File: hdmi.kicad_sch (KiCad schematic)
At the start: 43 parts, among them J13 WE_685119136923_alt_sym, Q1 PJE138K, Q12 PJE138K, U36 TS3DV642RUARQ1, U43 NTS0102GT, U44 TPD4E05U06QDQARQ1, U45 TPD4E05U06QDQARQ1, U46 TPD4E05U06QDQARQ1

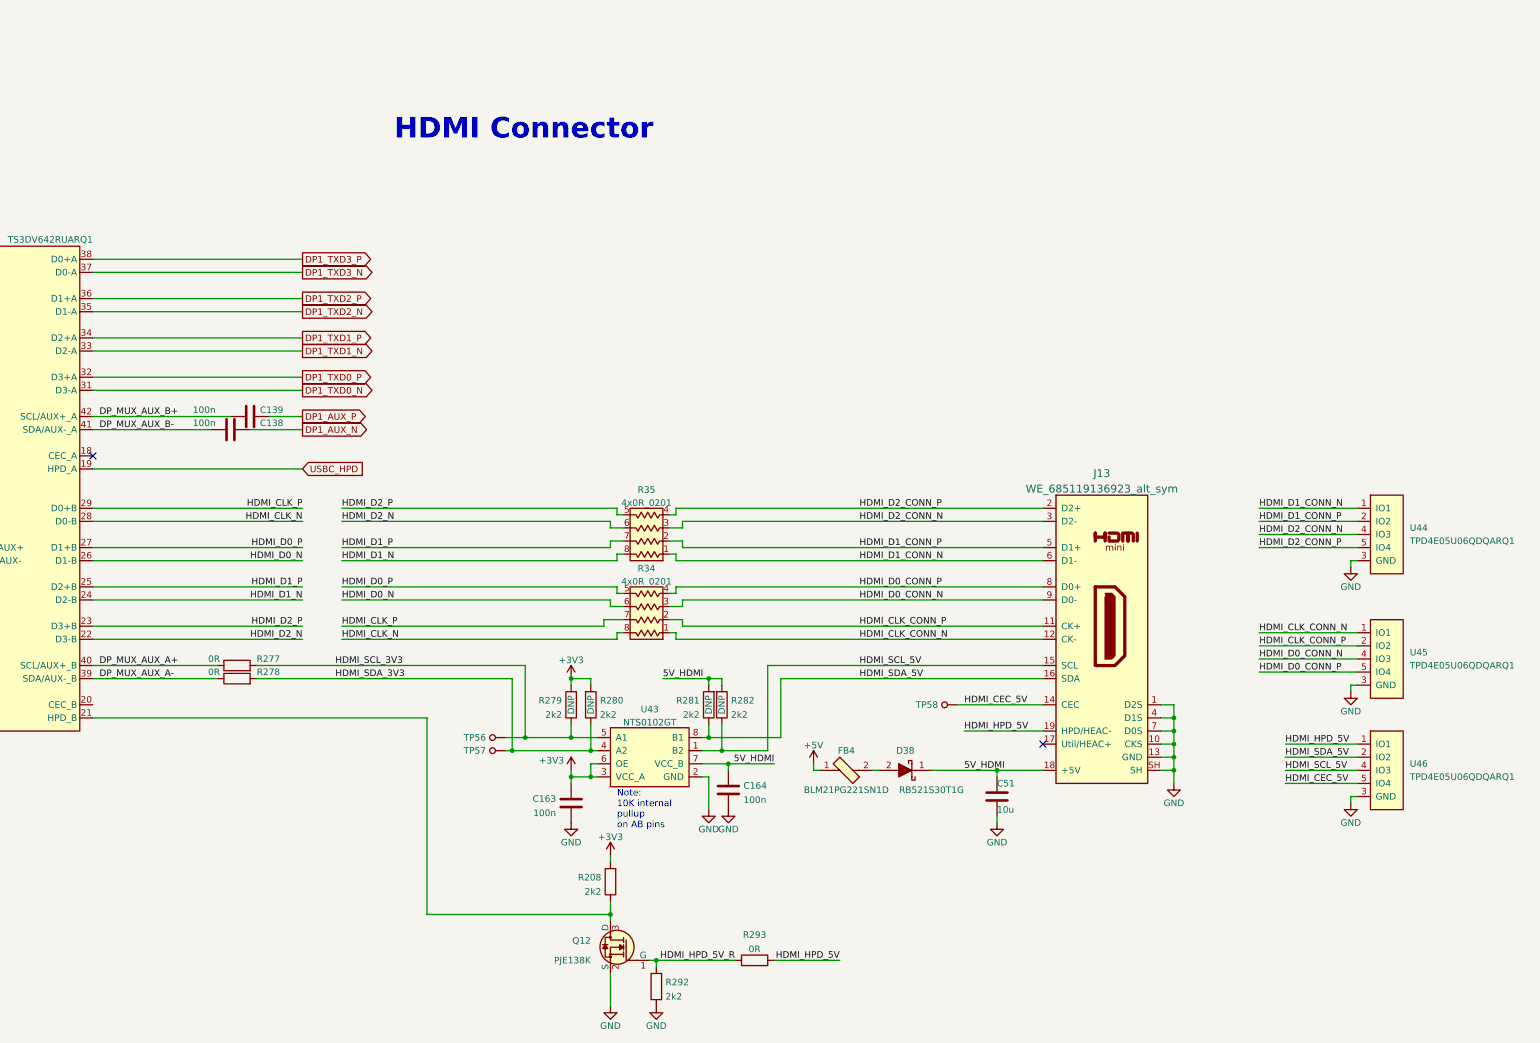
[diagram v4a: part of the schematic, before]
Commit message: Added 499 Ohm resistors required for HDMI
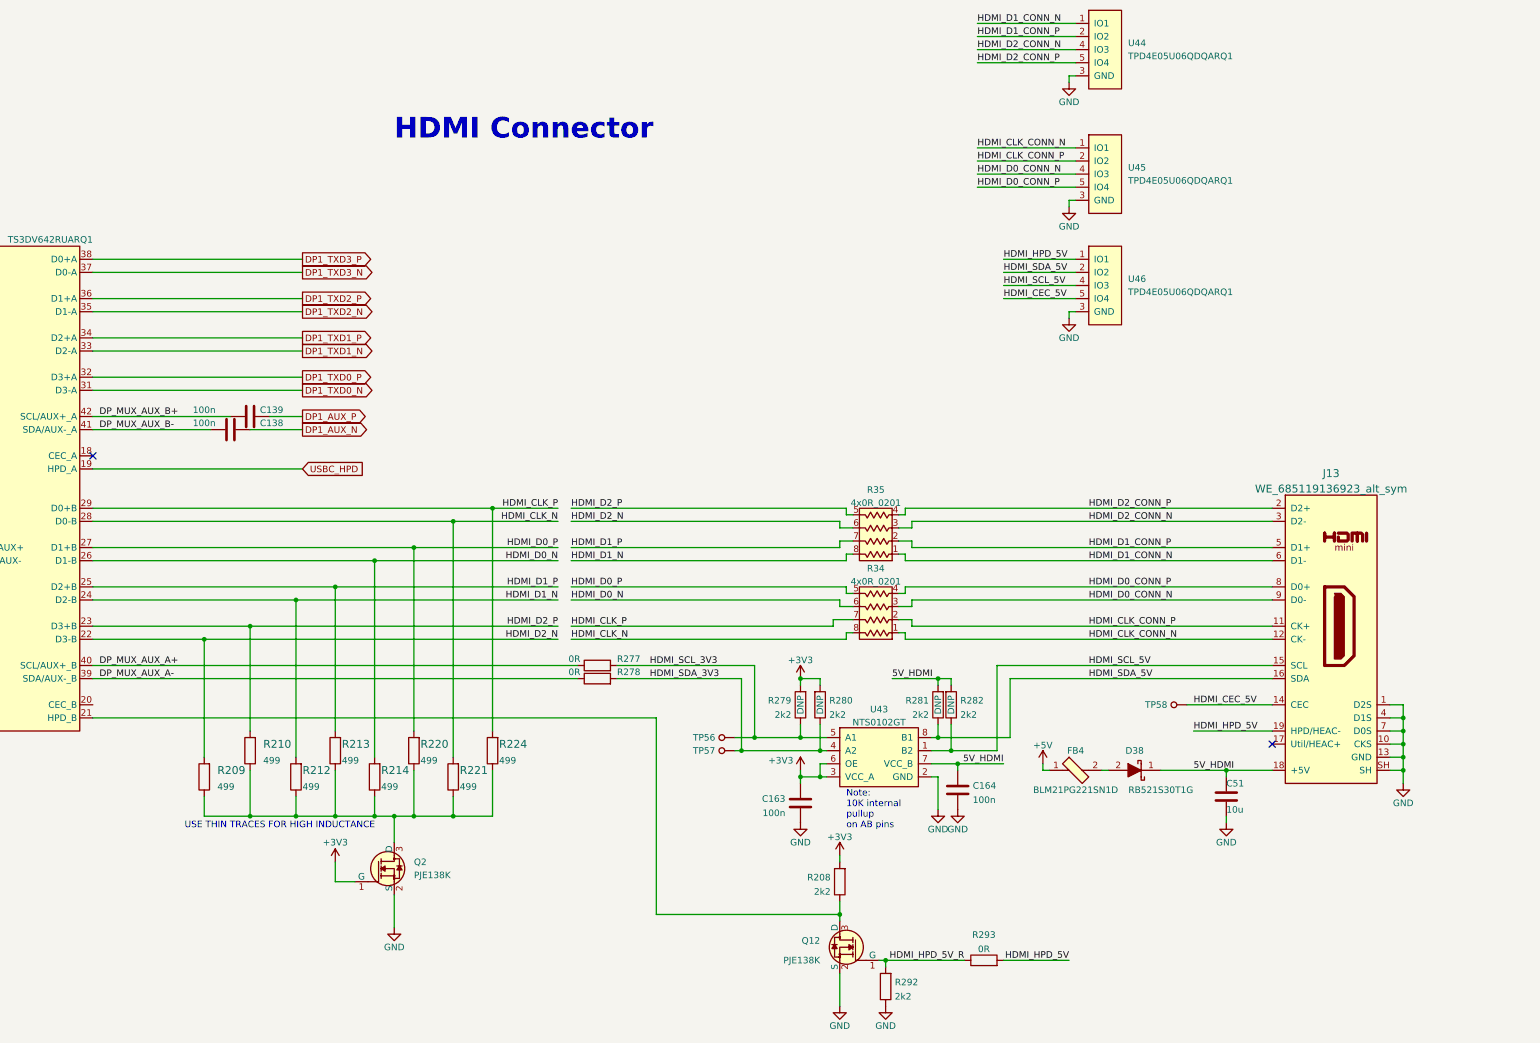
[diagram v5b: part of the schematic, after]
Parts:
- added Q2: PJE138K, antmicro-footprints:SOT-523, symbol antmicroTransistorsFETsMOSFETsSingle:PJE138K
- added R209, R210, R212, R213, R214, R220, R221, R224: R_499_0402, antmicro-footprints:0402-res, symbol antmicroResistors0402:R_499_0402
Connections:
- net +3V3: now also Q2.1 (G)
- net GND: now also Q2.2 (S)
- net HDMI_CLK_N: now also R221.2
- net HDMI_CLK_P: now also R224.2
- net HDMI_D0_N: now also R214.2
- net HDMI_D0_P: now also R220.2
- net HDMI_D1_N: now also R212.2
- net HDMI_D1_P: now also R213.2
- net HDMI_D2_N: now also R209.2
- net HDMI_D2_P: now also R210.2
- new net: Q2.3 (D), R209.1, R210.1, R212.1, R213.1, R214.1, R220.1, R221.1, R224.1
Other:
- note added: "USE THIN TRACES FOR HIGH INDUCTANCE"
- moved on the sheet: C163, C164, C51, D38, FB4, J13, Q12, R208, R277, R278, R279, R280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

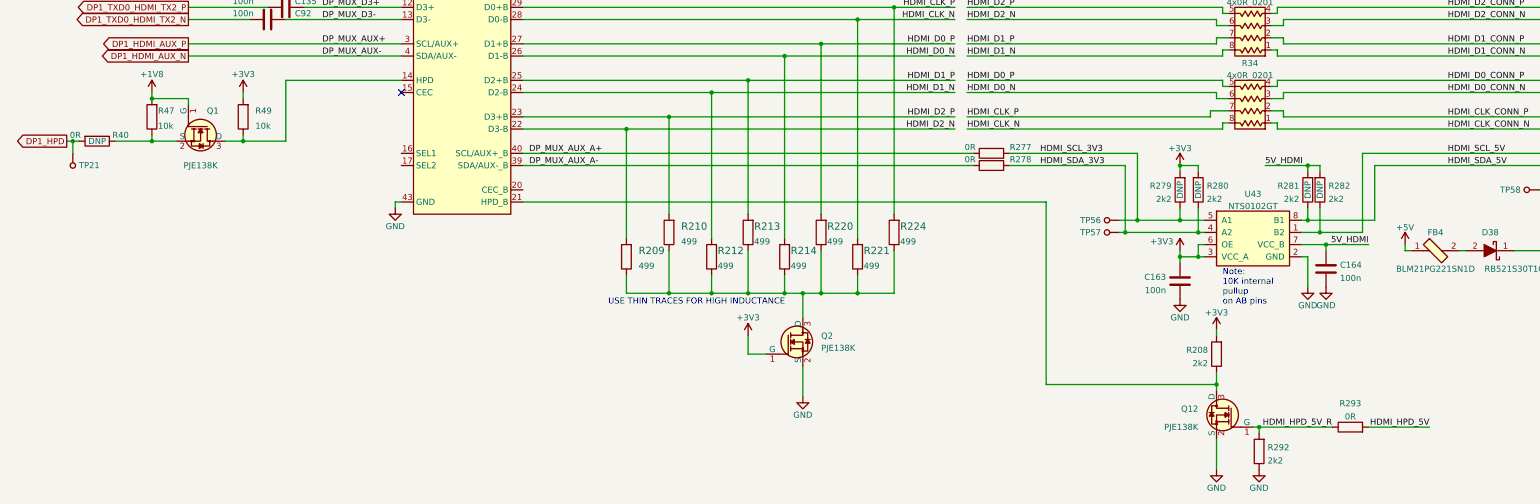
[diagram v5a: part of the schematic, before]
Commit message: Added switching logic for display mux
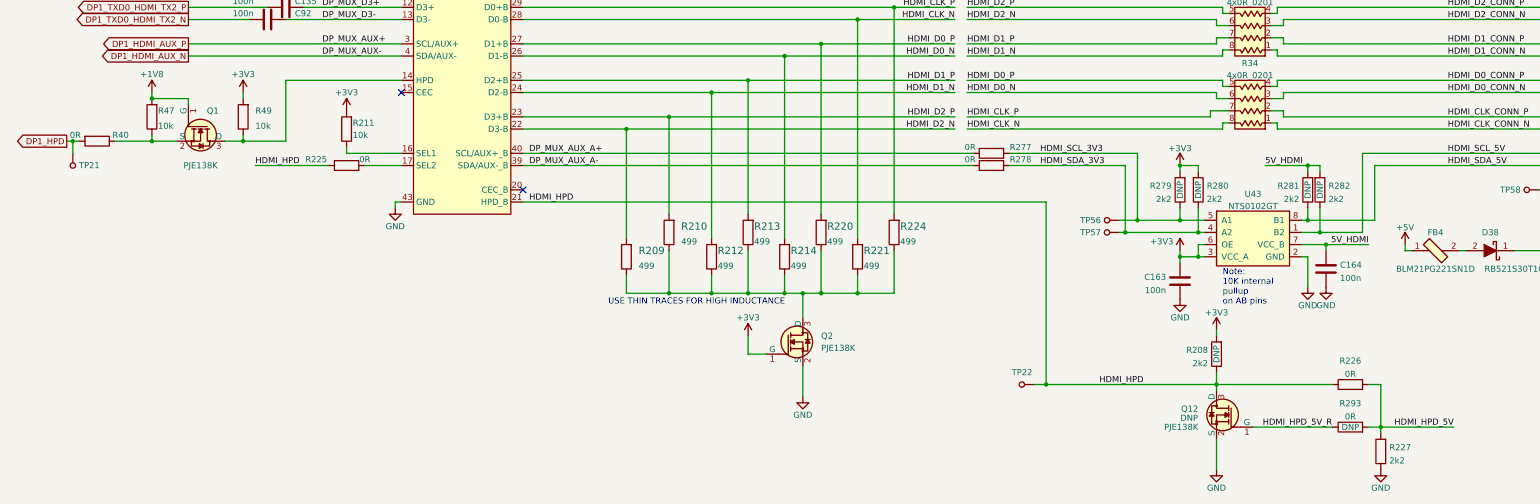
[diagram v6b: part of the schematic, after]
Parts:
- removed R292: R_2k2_0402, jetson-orin-baseboard-footprints:0402-res, symbol jetson-orin-baseboard:R_2k2_0402
- added R211: R_10k_0402, jetson-orin-baseboard-footprints:0402-res, symbol jetson-orin-baseboard:R_10k_0402
- added R225, R226: R_0R_0402, jetson-orin-baseboard-footprints:0402-res, symbol jetson-orin-baseboard:R_0R_0402
- added R227: R_2k2_0402, jetson-orin-baseboard-footprints:0402-res, symbol jetson-orin-baseboard:R_2k2_0402
- added TP22: TP_SMD_0_75MM, antmicro-footprints:Testpoint_smd_0_75mm, symbol antmicroTestPoints:TP_SMD_0_75MM
- Q12, R208, R293: DNP (none) -> DNP
- R40: DNP DNP -> (none)
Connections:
- net +3V3: now also R211.2
- net GND: now also R227.1
- net HDMI_HPD_5V: now also R226.2, R227.2
- net at U36.16 (SEL1): now also R211.1
- net at U36.17 (SEL2): now also R225.2
- net HDMI_HPD: now reaches Q12.3 (D), R208.1, U36.21 (HPD_B)
- net HDMI_HPD: now also R225.1, R226.1, TP22.1
- no-connect marks 3 -> 4

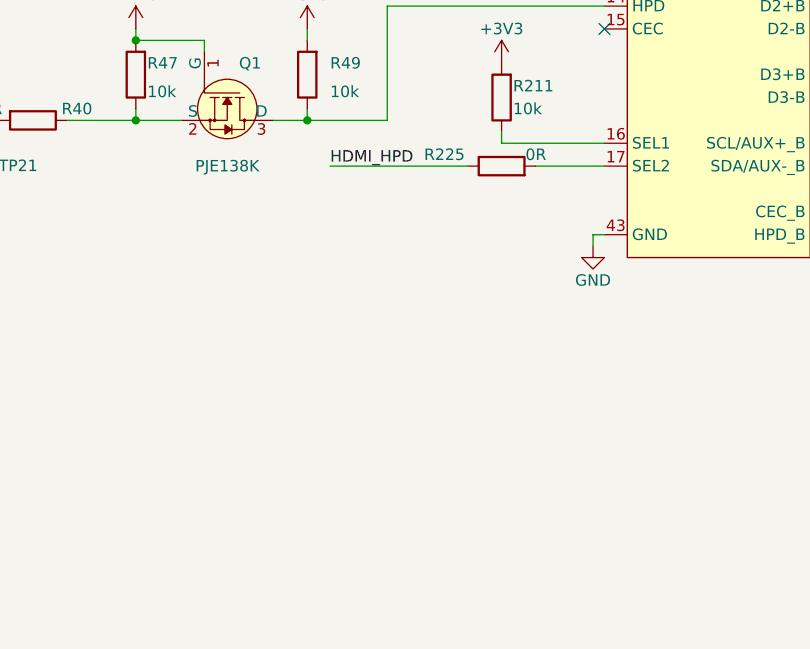
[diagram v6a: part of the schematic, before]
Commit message: Added alternative DNP circuitry to make DP priority
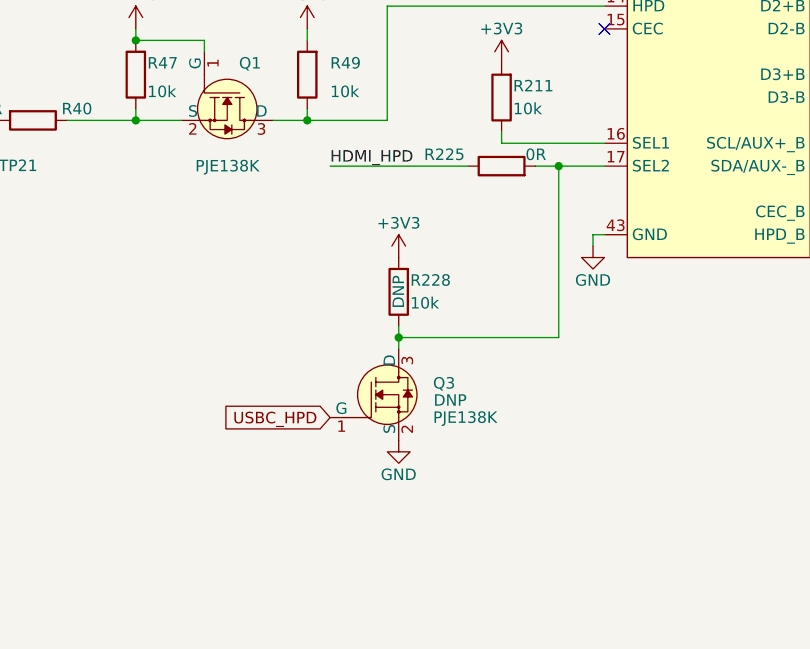
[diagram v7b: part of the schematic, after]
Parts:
- added Q3: PJE138K, antmicro-footprints:SOT-523, symbol antmicroTransistorsFETsMOSFETsSingle:PJE138K
- added R228: R_10k_0402, jetson-orin-baseboard-footprints:0402-res, symbol jetson-orin-baseboard:R_10k_0402
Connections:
- net +3V3: now also R228.2
- net GND: now also Q3.2 (S)
- net USBC_HPD: now also Q3.1 (G)
- net at R225.2, U36.17 (SEL2): now also Q3.3 (D), R228.1
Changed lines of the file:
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@@
   (junction (at 233.68 215.9) (diameter 0) (color 0 0 0 0)
   )
+  (junction (at 76.2 189.23) (diameter 0) (color 0 0 0 0)
+  )
   (junction (at 261.62 170.18) (diameter 0) (color 0 0 0 0)
   )
@@
   (junction (at 186.69 144.78) (diameter 0) (color 0 0 0 0)
   )
+  (junction (at 93.98 170.18) (diameter 0) (color 0 0 0 0)
+  )
   (junction (at 46.99 156.21) (diameter 0) (color 0 0 0 0)
   )
@@
     (stroke (width 0) (type default) (color 0 0 0 0))
   )
+  (wire (pts (xy 76.2 187.96) (xy 76.2 189.23))
+    (stroke (width 0) (type default) (color 0 0 0 0))
+  )
   (wire (pts (xy 300.99 91.44) (xy 314.96 91.44))
     (stroke (width 0) (type default) (color 0 0 0 0))
@@
     (stroke (width 0) (type default) (color 0 0 0 0))
   )
+  (wire (pts (xy 76.2 189.23) (xy 93.98 189.23))
+    (stroke (width 0) (type default) (color 0 0 0 0))
+  )
   (wire (pts (xy 281.94 138.43) (xy 280.67 138.43))
     (stroke (width 0) (type default) (color 0 0 0 0))
@@
     (stroke (width 0) (type default) (color 0 0 0 0))
   )
+  (wire (pts (xy 76.2 189.23) (xy 76.2 190.5))
+    (stroke (width 0) (type default) (color 0 0 0 0))
+  )
   (wire (pts (xy 54.61 132.08) (xy 67.31 132.08))
     (stroke (width 0) (type default) (color 0 0 0 0))
@@
     (stroke (width 0) (type default) (color 0 0 0 0))
   )
+  (wire (pts (xy 93.98 189.23) (xy 93.98 170.18))
+    (stroke (width 0) (type default) (color 0 0 0 0))
+  )
   (wire (pts (xy 171.45 196.85) (xy 179.07 196.85))
     (stroke (width 0) (type default) (color 0 0 0 0))
@@
     (stroke (width 0) (type default) (color 0 0 0 0))
   )
+  (wire (pts (xy 93.98 170.18) (xy 99.06 170.18))
+    (stroke (width 0) (type default) (color 0 0 0 0))
+  )
   (wire (pts (xy 146.05 162.56) (xy 146.05 185.42))
     (stroke (width 0) (type default) (color 0 0 0 0))
@@
     (stroke (width 0) (type default) (color 0 0 0 0))
   )
-  (wire (pts (xy 91.44 170.18) (xy 99.06 170.18))
+  (wire (pts (xy 91.44 170.18) (xy 93.98 170.18))
     (stroke (width 0) (type default) (color 0 0 0 0))
   )
@@
     )
   )
+  (global_label "USBC_HPD" (shape input) (at 68.58 198.12 180)
+    (effects (font (size 1.27 1.27)) (justify right))
+    (property "Intersheet References" "${INTERSHEET_REFS}" (id 0) (at 54.61 198.12 0)
+      (effects (font (size 1.27 1.27)) (justify right))
+    )
+  )
   (global_label "DP1_TXD0_P" (shape output) (at 165.1 111.76 0)
     (effects (font (size 1.27 1.27)) (justify left))
@@
     (pin "8")
   )
+  (symbol (lib_id "jetson-orin-baseboard:GND") (at 76.2 200.66 0) (unit 1)
+    (in_bom yes) (on_board yes) (fields_autoplaced)
+    (property "Reference" "#PWR0330" (id 0) (at 76.2 207.01 0)
+      (effects (font (size 1.27 1.27)) hide)
+    )
+    (property "Value" "GND" (id 1) (at 76.2 204.47 0))
+    (property "Footprint" "" (id 2) (at 76.2 200.66 0)
+      (effects (font (size 1.27 1.27)) hide)
+    )
+    (property "Datasheet" "" (id 3) (at 76.2 200.66 0)
+      (effects (font (size 1.27 1.27)) hide)
+    )
+    (pin "1")
+  )
+  (symbol (lib_id "jetson-orin-baseboard:R_10k_0402") (at 76.2 184.15 90) (unit 1)
+    (in_bom yes) (on_board yes)
+    (property "Reference" "R228" (id 0) (at 77.47 182.88 90)
+      (effects (font (size 1.27 1.27)) (justify right))
+    )
+    (property "Value" "R_10k_0402" (id 1) (at 80.01 184.15 0)
+      (effects (font (size 1.27 1.27)) hide)
+    )
+    (property "Footprint" "jetson-orin-baseboard-footprints:0402-res" (id 2) (at 71.12 179.07 0)
+      (effects (font (size 1.524 1.524)) (justify left) hide)
+    )
+    (property "Datasheet" "" (id 3) (at 76.2 184.15 0)
+      (effects (font (size 1.27 1.27)) hide)
+    )
+    (property "Manufacturer" "VISHAY" (id 4) (at 66.04 179.07 0)
+      (effects (font (size 1.524 1.524)) (justify left) hide)
+    )
+    (property "MPN" "CRCW040210K0FKEDHP" (id 5) (at 68.58 179.07 0)
+      (effects (font (size 1.524 1.524)) (justify left) hide)
+    )
+    (property "Val" "10k" (id 6) (at 77.47 185.4169 90)
+      (effects (font (size 1.27 1.27)) (justify right))
+    )
+    (property "DNP" "DNP" (id 7) (at 76.2 184.15 0))
+    (pin "1")
+    (pin "2")
+  )
   (symbol (lib_id "antmicroResistors0402:R_499_0402") (at 163.83 189.23 90) (unit 1)
     (in_bom yes) (on_board yes)
@@
     (pin "2")
   )
+  (symbol (lib_id "jetson-orin-baseboard:+3V3") (at 76.2 180.34 0) (unit 1)
+    (in_bom yes) (on_board yes)
+    (property "Reference" "#PWR0329" (id 0) (at 76.2 184.15 0)
+      (effects (font (size 1.27 1.27)) hide)
+    )
+    (property "Value" "+3V3" (id 1) (at 76.2 176.53 0))
+    (property "Footprint" "" (id 2) (at 76.2 180.34 0)
+      (effects (font (size 1.27 1.27)) hide)
+    )
+    (property "Datasheet" "" (id 3) (at 76.2 180.34 0)
+      (effects (font (size 1.27 1.27)) hide)
+    )
+    (pin "1")
+  )
   (symbol (lib_id "jetson-orin-baseboard:RB521S30T1G") (at 326.39 187.96 0) (unit 1)
     (in_bom yes) (on_board yes)
@@
     (pin "1")
   )
+  (symbol (lib_id "antmicroTransistorsFETsMOSFETsSingle:PJE138K") (at 76.2 195.58 0) (unit 1)
+    (in_bom yes) (on_board yes)
+    (property "Reference" "Q3" (id 0) (at 80.01 194.31 0)
+      (effects (font (size 1.27 1.27)) (justify left))
+    )
+    (property "Value" "PJE138K" (id 1) (at 80.01 198.12 0)
+      (effects (font (size 1.27 1.27)) (justify left))
+    )
+    (property "Footprint" "antmicro-footprints:SOT-523" (id 2) (at 81.28 190.5 0)
+      (effects (font (size 1.524 1.524)) (justify left) hide)
+    )
+    (property "Datasheet" "https://www.mouser.pl/datasheet/2/1057/PJE138K-1876698.pdf" (id 3) (at 81.28 187.96 0)
+      (effects (font (size 1.524 1.524)) (justify left) hide)
+    )
+    (property "MPN" "PJE138K_R1_00001" (id 4) (at 92.71 185.42 0)
+      (effects (font (size 1.524 1.524)) (justify left) hide)
+    )
+    (property "Manufacturer" "Panjit" (id 5) (at 81.28 185.42 0)
+      (effects (font (size 1.524 1.524)) (justify left) hide)
+    )
+    (property "DNP" "DNP" (id 6) (at 81.915 196.215 0))
+    (pin "1")
+    (pin "2")
+    (pin "3")
+  )
   (symbol (lib_id "antmicroResistors0402:R_499_0402") (at 146.05 189.23 90) (unit 1)
